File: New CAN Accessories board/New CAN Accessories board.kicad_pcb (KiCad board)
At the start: 2 copper layers, 106 x 91 mm, 101 parts, among them J1 39301040, J10 39301040, J11 ATF13-2P-BM03, J12 Conn_01x02_Pin, J2 39301040, J3 39301040, J4 39301040, J5 39301040, J6 39301040, J7 39301040, J8 39301040, J9 39301060, Q1 IRLML6344TRPBF, Q2 IRLML6344TRPBF, Q3 IRLML6344TRPBF, Q4 IRLML6344TRPBF, Q5 IRLML6344TRPBF, Q6 IRLML6344TRPBF, Q7 IRLML6344TRPBF, Q8 IRLML6344TRPBF, T1 MCP2562FD-E_SN, U1 NUCLEO_L432KC

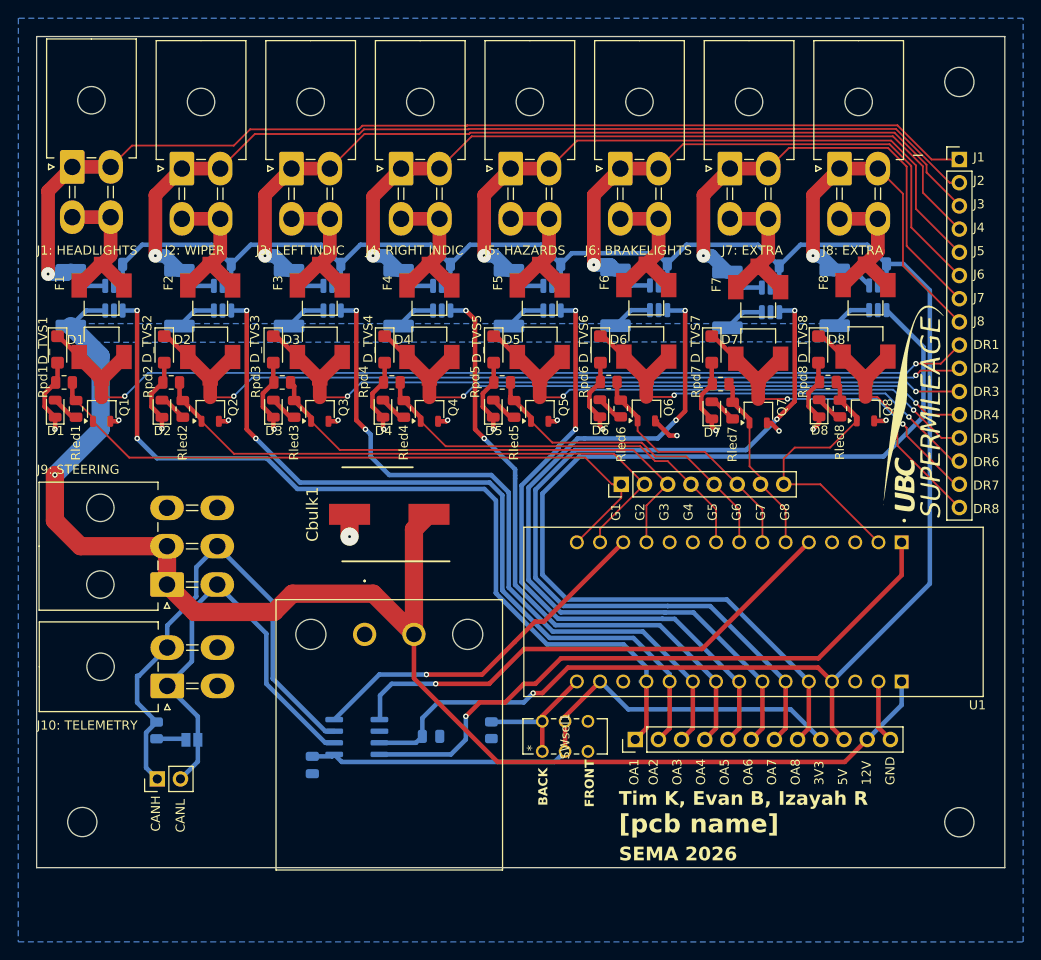
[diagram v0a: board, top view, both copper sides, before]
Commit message: updated diode placement
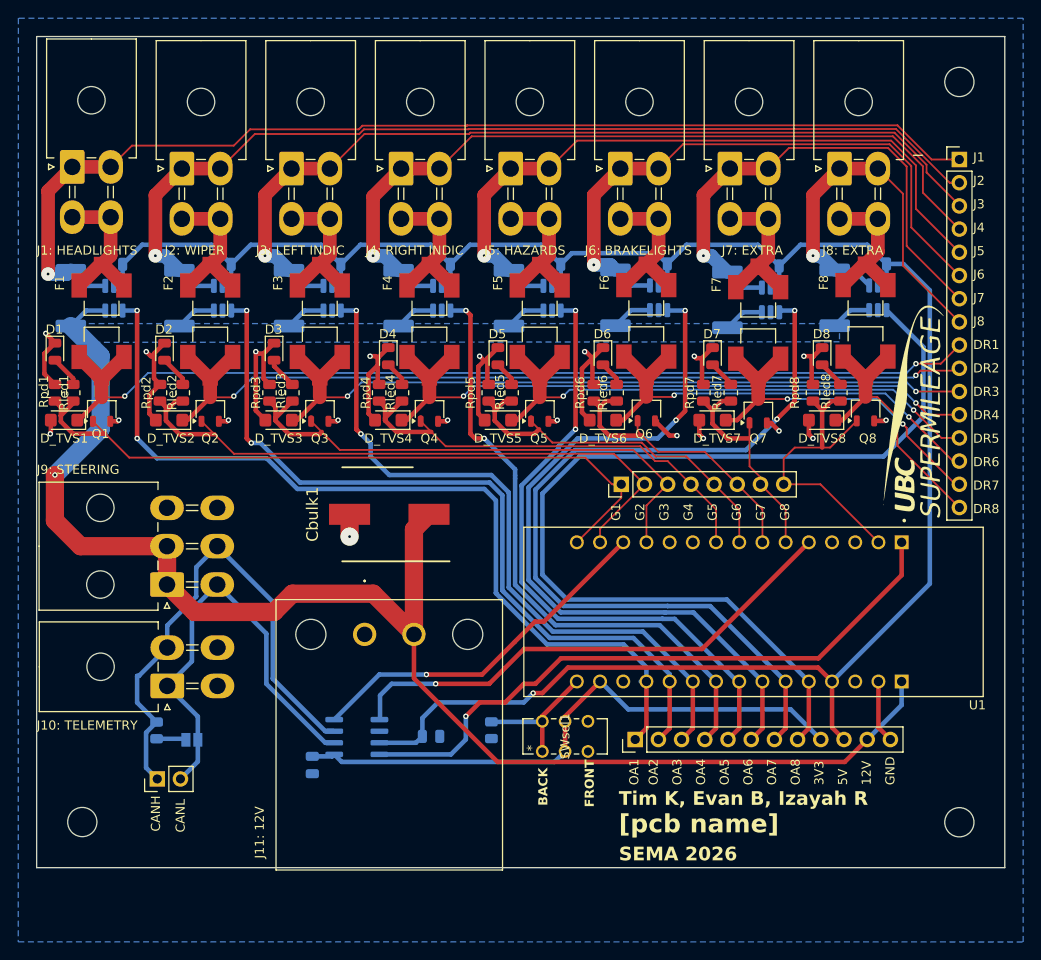
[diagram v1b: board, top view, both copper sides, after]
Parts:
- moved D_TVS1 7.77 mm to (19.0, 58.0), turned to 180 degrees
- moved D_TVS3 7.76 mm to (42.5, 58.0), turned to 180 degrees
- moved D_TVS2 7.76 mm to (30.5, 58.0), turned to 180 degrees
- moved D_TVS5 7.75 mm to (66.5, 58.0), turned to 180 degrees
- moved D_TVS8 7.75 mm to (102.0, 58.0), turned to 180 degrees
- moved D_TVS4 7.75 mm to (54.5, 58.0), turned to 180 degrees
- moved D_TVS6 7.74 mm to (78.0, 58.0), turned to 180 degrees
- moved D_TVS7 7.74 mm to (90.0, 58.0), turned to 180 degrees
- moved D2 6.25 mm to (30.0, 50.5), turned to -90 degrees
- moved D3 6.24 mm to (42.0, 50.5), turned to -90 degrees
- moved D1 6.24 mm to (18.0, 50.5), turned to -90 degrees
- moved D7 5.93 mm to (90.0, 51.0), turned to -90 degrees
- moved D4 5.77 mm to (54.5, 51.0), turned to -90 degrees
- moved D5 5.76 mm to (66.5, 51.0), turned to -90 degrees
- moved D6 5.71 mm to (78.0, 51.0), turned to -90 degrees
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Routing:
- net GND: track 88.6 -> 108.3 mm, vias 17 -> 20
- net /GATE3: track 54.4 -> 60.7 mm
- net /GATE4: track 45.1 -> 51.2 mm
- net /GATE2: track 65.0 -> 70.6 mm
- net /GATE5: track 35.6 -> 41.2 mm
- net /GATE6: track 27.1 -> 32.6 mm
- net /GATE1: track 74.3 -> 79.6 mm
- net /GATE7: track 19.9 -> 25.1 mm
- net /GATE8: track 31.3 -> 34.0 mm
- net /TPdr6: track 49.9 -> 50.8 mm
- net /TPdr7: track 39.1 -> 39.8 mm
- net /TPdr8: track 29.7 -> 30.4 mm
- net /TPdr4: track 72.2 -> 72.9 mm
- net /TPdr5: track 60.9 -> 61.6 mm
- net /OA4: track 67.2 -> 67.8 mm
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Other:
- board text added: "J11: 12V"
- board text removed: "D1"
- board text removed: "D2"
- board text removed: "D3"
- board text removed: "D4"
- board text removed: "D5"
- board text removed: "D6"
- board text removed: "D7"
- board text removed: "D8"

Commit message: finalized PCB design
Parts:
- J12: value Conn_01x02_Pin -> Conn_01x03_Pin; footprint Connector_PinHeader_2.54mm:PinHeader_1x02_P2.54mm_Vertical -> Connector_PinHeader_2.54mm:PinHeader_1x03_P2.54mm_Vertical
- moved J12 1.95 mm to (31.1, 97.3)
- moved JP1 0.85 mm to (32.5, 93.7)
- moved G*** 0.78 mm to (111.8, 57.8)
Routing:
- net GND: track 108.3 -> 113.5 mm, vias 20 -> 17
- net 12V: track 190.1 -> 186.7 mm
- net /OA8: track 108.3 -> 110.7 mm
- net /GATE4: track 51.2 -> 53.4 mm
- net 5V: track 229.2 -> 230.6 mm
- net /CANL: track 49.1 -> 48.1 mm
- net /CANH: track 57.2 -> 58.0 mm
- net /OA6: track 80.8 -> 80.1 mm
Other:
- board text added: "12V"
- board text added: "12V PWR"
- board text added: "GND"
- board text added: "J11"
- board text added: "{dblquote}J.G.{dblquote}"
- board text added: "{dblquote}Lvl.99 MOSFET Destroyer{dblquote}"
- board text removed: "J11: 12V"
- board text removed: "[pcb name]"

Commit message: final final design (changed a couple traces)
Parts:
- moved D1 0.70 mm to (18.7, 50.5)
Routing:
- net /TPj1: track 120.5 -> 118.8 mm
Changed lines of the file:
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@@
 	(footprint "LED_SMD:LED_0805_2012Metric"
 		(layer "F.Cu")
-		(at 18 50.5 -90)
+		(at 18.7 50.5 -90)
 		(descr "LED SMD 0805 (2012 Metric), square (rectangular) end terminal, IPC-7351 nominal, (Body size source: https://docs.google.com/spreadsheets/d/1BsfQQcO9C6DZCsRaXUlFlo91Tg2WpOkGARC1WS5S8t0/edit?usp=sharing), generated with kicad-footprint-generator")
 		(tags "LED")
@@
 	)
 	(segment
-		(start 18 49.5625)
-		(end 16.849 50.7135)
-		(width 0.5)
-		(layer "F.Cu")
-		(net 1)
-	)
-	(segment
 		(start 54.5 50.0625)
 		(end 53.349 51.2135)
@@
 	)
 	(segment
+		(start 17.05 50.5125)
+		(end 17.05 53.1375)
+		(width 0.5)
+		(layer "F.Cu")
+		(net 1)
+	)
+	(segment
 		(start 19.2 61.1)
 		(end 17.55 59.45)
@@
 	)
 	(segment
-		(start 18 49.5625)
-		(end 18 49.5)
-		(width 0.5)
-		(layer "F.Cu")
-		(net 1)
-	)
-	(segment
 		(start 101 54.0875)
 		(end 99.849 55.2385)
@@
 	)
 	(segment
+		(start 18 49.5)
+		(end 18 49.5625)
+		(width 0.5)
+		(layer "F.Cu")
+		(net 1)
+	)
+	(segment
 		(start 24.06 58.125)
 		(end 24.875 58.125)
@@
 	)
 	(segment
+		(start 18 49.5625)
+		(end 17.05 50.5125)
+		(width 0.5)
+		(layer "F.Cu")
+		(net 1)
+	)
+	(segment
 		(start 95.95 58.31)
 		(end 96.41 58.31)
@@
 	)
 	(segment
-		(start 16.849 50.7135)
-		(end 16.849 52.9365)
-		(width 0.5)
-		(layer "F.Cu")
-		(net 1)
-	)
-	(segment
-		(start 16.849 52.9365)
-		(end 18 54.0875)
-		(width 0.5)
-		(layer "F.Cu")
-		(net 1)
-	)
-	(segment
 		(start 28.349 57.299)
 		(end 29.05 58)
@@
 	)
 	(segment
+		(start 17.05 53.1375)
+		(end 18 54.0875)
+		(width 0.5)
+		(layer "F.Cu")
+		(net 1)
+	)
+	(segment
 		(start 102 50.0625)
 		(end 101.03125 51.03125)
@@
 	)
 	(segment
-		(start 17.251 32.924)
-		(end 17.251 42)
-		(width 1.5)
-		(layer "F.Cu")
-		(net 59)
-	)
-	(segment
 		(start 26.435 27.94)
 		(end 24.1 30.275)
@@
 	(segment
 		(start 19.9 30.275)
-		(end 17.251 32.924)
-		(width 1.5)
-		(layer "F.Cu")
-		(net 59)
-	)
-	(segment
-		(start 19.9 30.275)
 		(end 24.1 30.275)
 		(width 1.5)
@@
 	)
 	(segment
+		(start 17.571 40.03)
+		(end 17.41 39.869)
+		(width 1.5)
+		(layer "F.Cu")
+		(net 59)
+	)
+	(segment
 		(start 113.99144 29.464)
 		(end 110.24844 25.721)
@@
 	)
 	(segment
+		(start 17.41 39.869)
+		(end 17.41 32.765)
+		(width 1.5)
+		(layer "F.Cu")
+		(net 59)
+	)
+	(segment
+		(start 17.41 32.765)
+		(end 19.9 30.275)
+		(width 1.5)
+		(layer "F.Cu")
+		(net 59)
+	)
+	(segment
 		(start 37.592 27.94)
 		(end 26.435 27.94)
@@
 		(net 59)
 	)
+	(segment
+		(start 17.64 40.03)
+		(end 17.571 40.03)
+		(width 1.5)
+		(layer "F.Cu")
+		(net 59)
+	)
 	(via
-		(at 17.251 42)
+		(at 17.64 40.03)
 		(size 1.5)
 		(drill 0.3)
@@
 	)
 	(segment
-		(start 17.251 42)
-		(end 19.34 42)
+		(start 23.513 43.3)
+		(end 21.44 43.3)
+		(width 0.5)
+		(layer "B.Cu")
+		(net 59)
+	)
+	(segment
+		(start 17.64 40.099)
+		(end 19.141 41.6)
 		(width 1.5)
 		(layer "B.Cu")
@@
 	)
 	(segment
-		(start 19.34 42)
+		(start 19.141 41.6)
 		(end 19.74 41.6)
 		(width 1.5)
@@
 	)
 	(segment
-		(start 23.513 43.3)
-		(end 21.44 43.3)
-		(width 0.5)
+		(start 17.64 40.03)
+		(end 17.64 40.099)
+		(width 1.5)
 		(layer "B.Cu")
 		(net 59)
